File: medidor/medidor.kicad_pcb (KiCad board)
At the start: 2 copper layers, 55 x 80 mm, 26 parts, among them J1 Screw_Terminal_01x02, J2 Conn_01x01_Female, J3 Conn_01x01_Female, J4 Conn_01x06, J5 Screw_Terminal_01x02, U1 LTC1966CMS8PBF, U2 MCP6001U

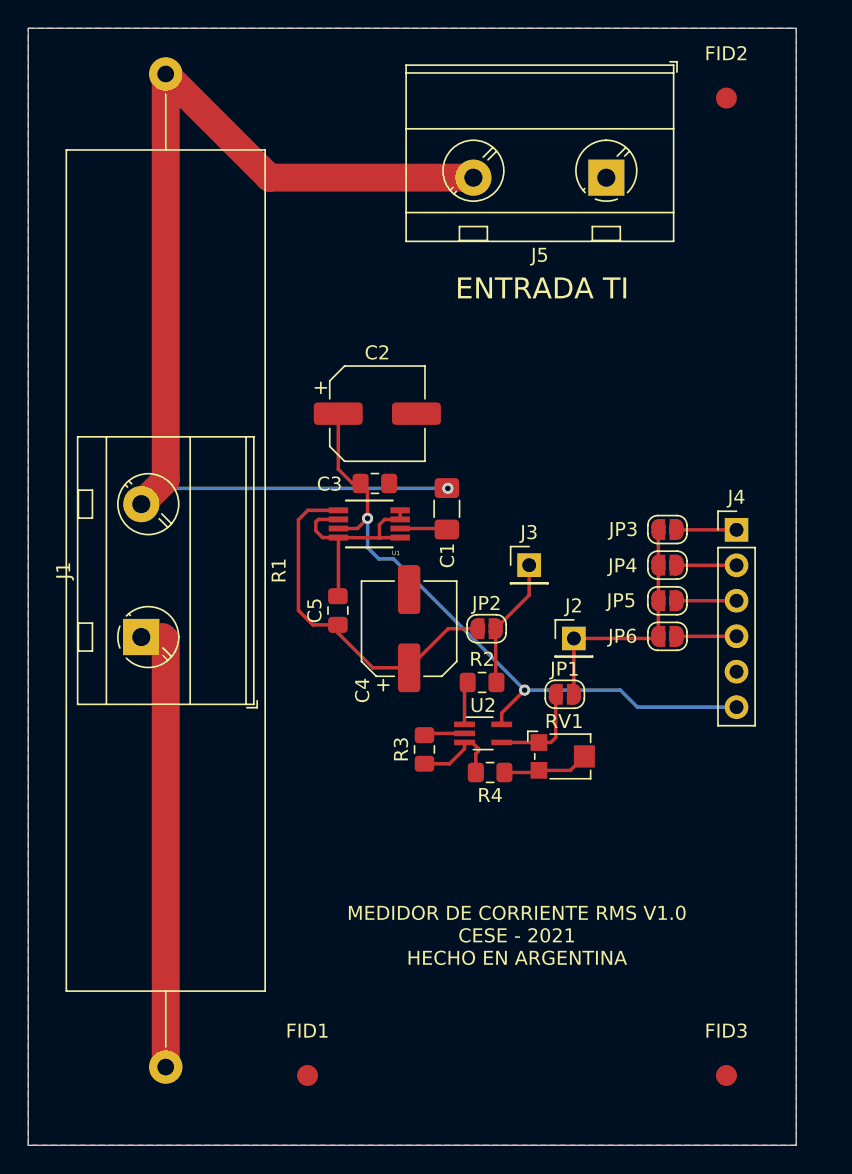
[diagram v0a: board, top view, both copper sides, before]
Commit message: Se agregan correcciones sugeridas por el docente y se define la version con shunt TO-220-2
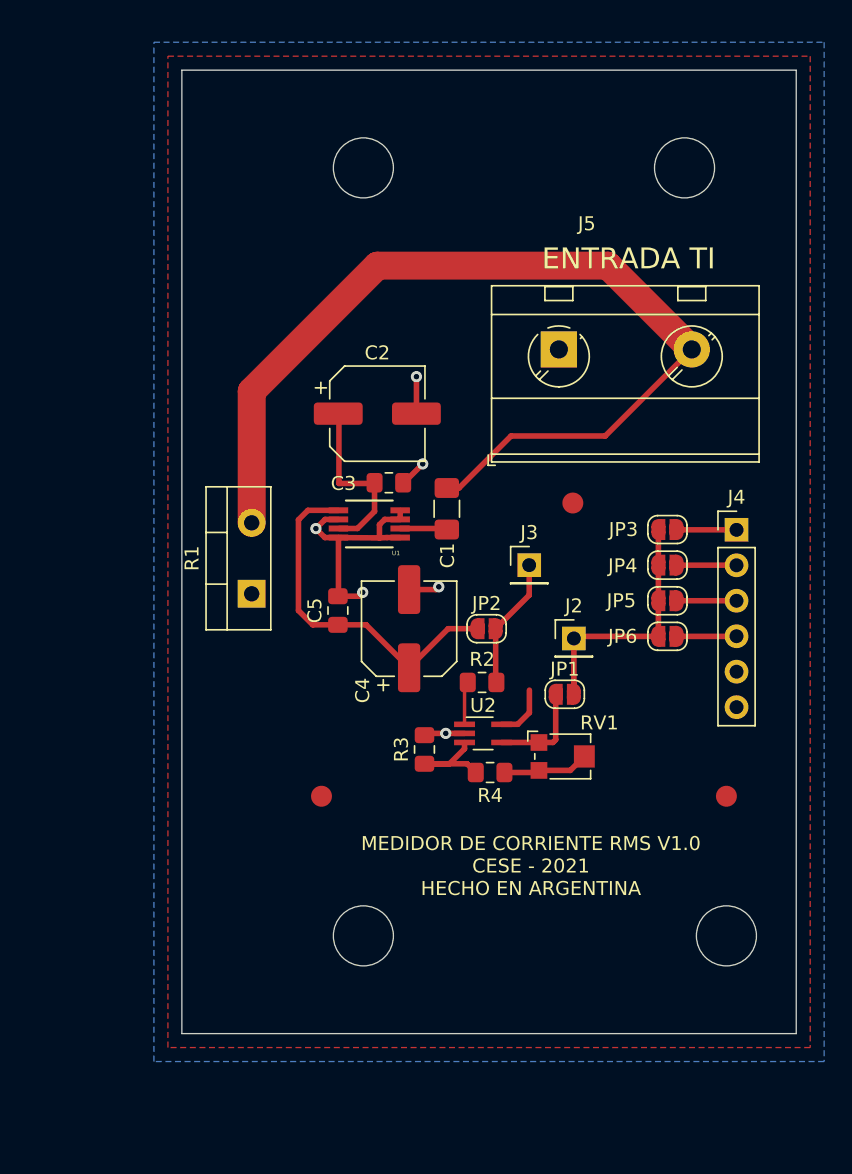
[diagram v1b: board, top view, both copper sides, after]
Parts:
- removed J1: Screw_Terminal_01x02, TerminalBlock_MetzConnect:TerminalBlock_MetzConnect_Type703_RT10N02HGLU_1x02_P9.52mm_Horizontal
- added H1: MountingHole, MountingHole:MountingHole_4.3mm_M4, F.Cu at (150.0, 120.0)
- added H2: MountingHole, MountingHole:MountingHole_4.3mm_M4, F.Cu at (124.0, 65.0)
- added H3: MountingHole, MountingHole:MountingHole_4.3mm_M4, F.Cu at (124.0, 120.0)
- added H4: MountingHole, MountingHole:MountingHole_4.3mm_M4, F.Cu at (147.0, 65.0)
- R1: footprint Resistor_THT:R_Axial_Power_L60.0mm_W14.0mm_P71.12mm -> TO_220_2_THT:TO-220-2_Vertical
- RV1: value R_POT -> 5k
- moved R1 37.7 mm to (116.0, 95.5), turned to 90 degrees
- moved FID2 31.0 mm to (139.0, 89.0)
- moved FID1 20.0 mm to (121.0, 110.0)
- moved FID3 20.0 mm to (150.0, 110.0)
- moved J5 12.8 mm to (138.0, 78.0), turned to 0 degrees
- moved C3 1.00 mm to (125.8, 87.5)
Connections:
- R1 pad 1: /CT_INPUT_2 -> GND
- R1 pad 2: GND -> /CT_INPUT_2
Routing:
- net VDD: track 47.5 -> 16.7 mm, vias 2 -> 0
- net GND: track 51.4 -> 27.3 mm, vias 0 -> 6
- net /CT_INPUT_2: track 79.1 -> 68.9 mm, vias 1 -> 0
- net Net-(R3-Pad1): track 6.73 -> 7.70 mm
- added copper zone on F.Cu, net VDD
- removed copper zone on F.Cu, net GND
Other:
- board size 55 x 80 mm -> 44 x 69 mm
- board text added: "NOTAS AL FABRICANTE Minimo ancho de pista: 0,25mm Minimo diamtero via: 0,8 mm Minimo taladro: 0.4 mm Margen borde: 0,5 mm Clearance minimo: 0,2mm Grillas: 0.05mm 0.5mm 1mm 5mm Terminacion: HASL Valores tomados en base a fabricante: Mayer PCB"
- board text removed: "NOTAS AL FABRICANTE VIAS: 0.8mm VIA DRILL: 0.4mm PISTAS: 0.25mm Y 2 mm"
